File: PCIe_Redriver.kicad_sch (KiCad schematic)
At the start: 56 parts, among them U10 SN75LVPE4410RNQR, U9 SN75LVPE4410RNQR

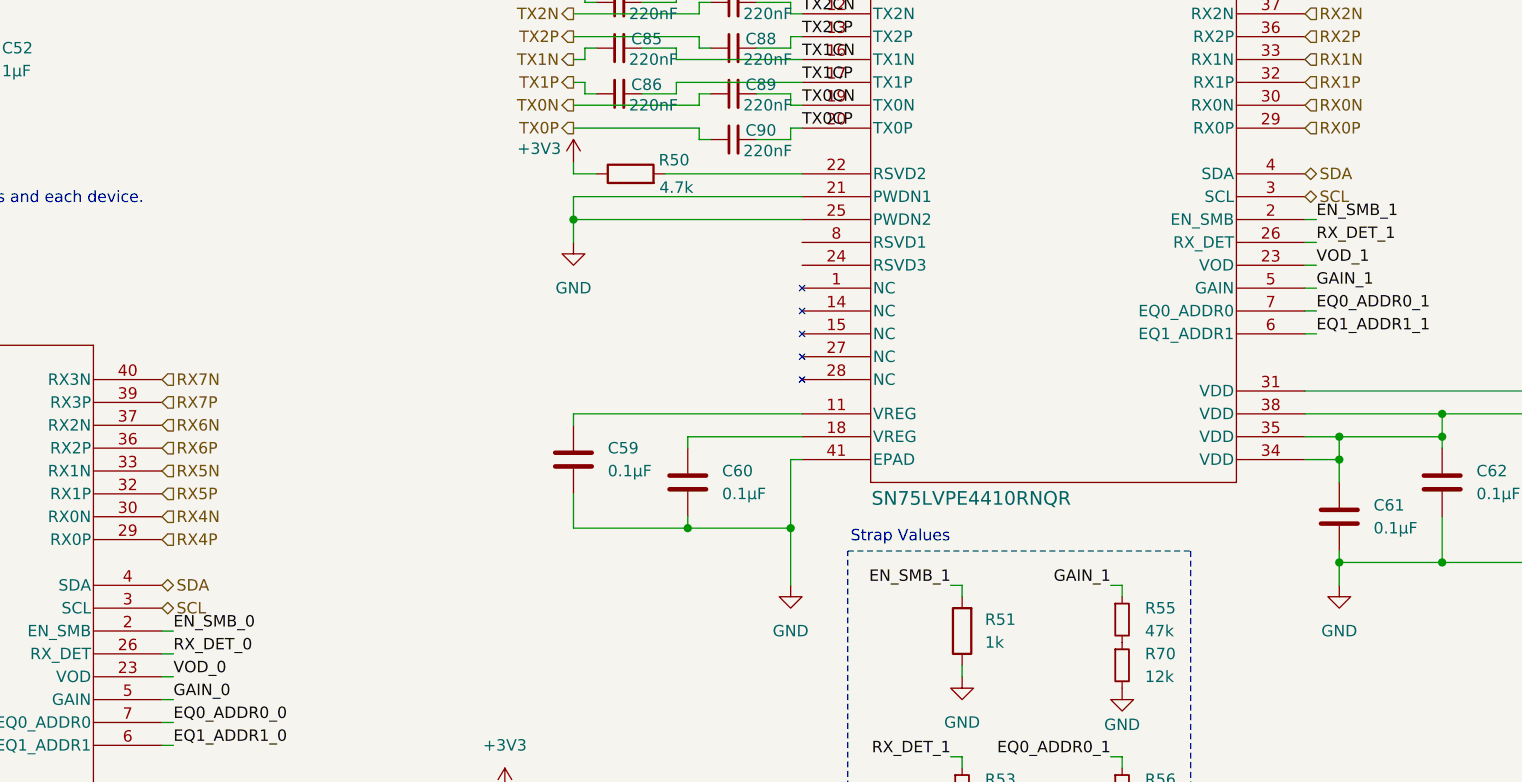
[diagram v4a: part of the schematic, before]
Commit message: Fixed all DRC errors
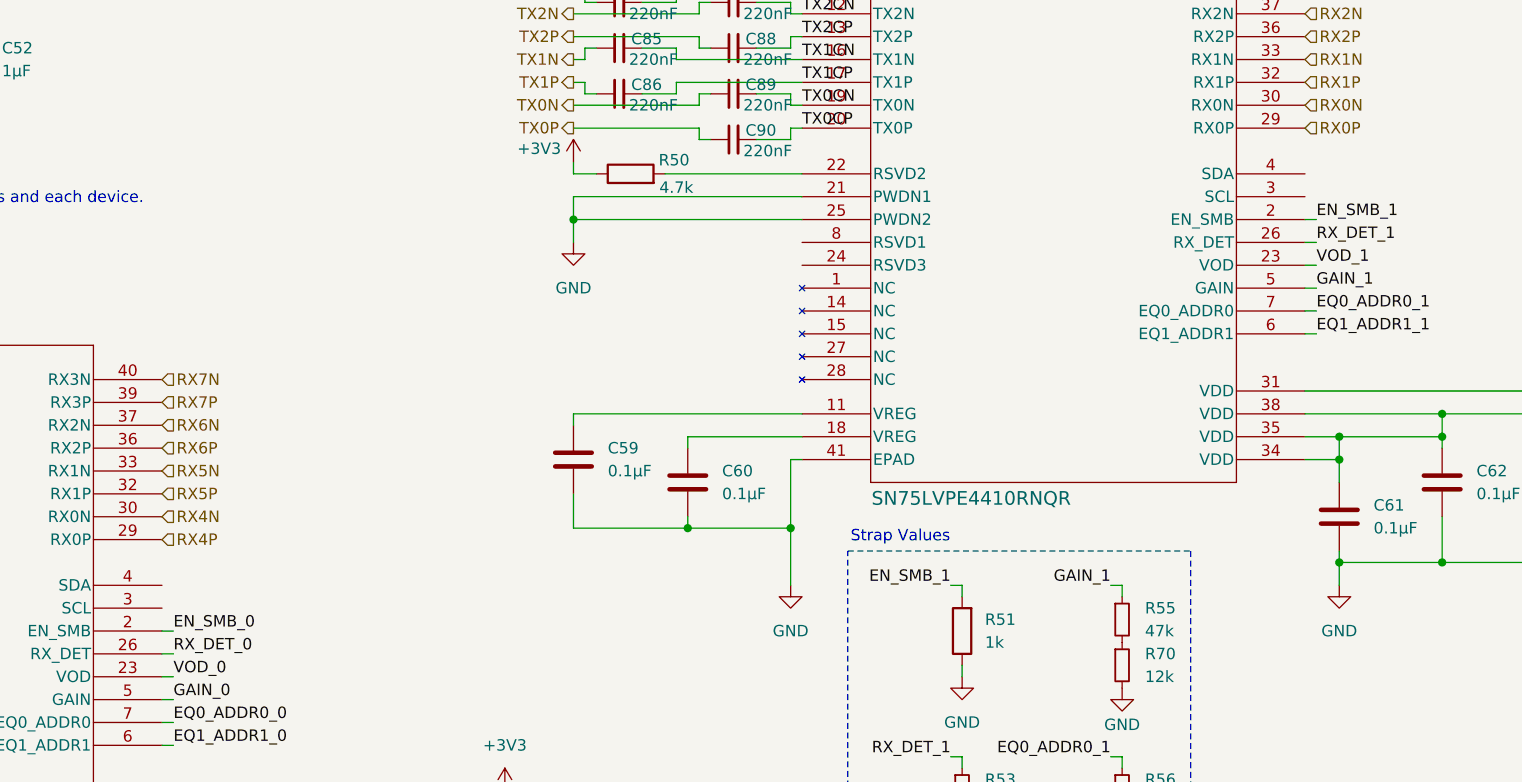
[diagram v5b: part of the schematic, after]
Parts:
- U10, U9: footprint SN75LVPE4410RNQR -> SN75LVPE4410RNQR:SN75LVPE4410RNQR
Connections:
- net SCL: no longer names the net of U9.3 (SCL)
- net SCL: no longer U10.3 (SCL)
- net SDA: no longer names the net of U9.4 (SDA)
- net SDA: no longer U10.4 (SDA)
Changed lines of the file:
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@@
 		)
 	)
-	(hierarchical_label "SDA"
-		(shape bidirectional)
-		(at 107.95 92.71 0)
-		(fields_autoplaced yes)
-		(effects
-			(font
-				(size 1.27 1.27)
-			)
-			(justify left)
-		)
-	)
 	(hierarchical_label "TX3N"
 		(shape output)
@@
 		)
 	)
-	(hierarchical_label "SCL"
-		(shape bidirectional)
-		(at 234.95 49.53 0)
-		(fields_autoplaced yes)
-		(effects
-			(font
-				(size 1.27 1.27)
-			)
-			(justify left)
-		)
-	)
 	(hierarchical_label "TX5N"
 		(shape output)
@@
 		)
 	)
-	(hierarchical_label "SCL"
-		(shape bidirectional)
-		(at 107.95 95.25 0)
-		(fields_autoplaced yes)
-		(effects
-			(font
-				(size 1.27 1.27)
-			)
-			(justify left)
-		)
-	)
 	(hierarchical_label "TX6N"
 		(shape output)
@@
 		)
 	)
-	(hierarchical_label "SDA"
-		(shape bidirectional)
-		(at 234.95 46.99 0)
-		(fields_autoplaced yes)
-		(effects
-			(font
-				(size 1.27 1.27)
-			)
-			(justify left)
-		)
-	)
 	(hierarchical_label "TX2P"
 		(shape output)
@@
 			)
 		)
-		(property "Footprint" "SN75LVPE4410RNQR"
+		(property "Footprint" "SN75LVPE4410RNQR:SN75LVPE4410RNQR"
 			(at 52.07 71.12 0)
 			(effects
@@
 			)
 		)
-		(property "Footprint" "SN75LVPE4410RNQR"
+		(property "Footprint" "SN75LVPE4410RNQR:SN75LVPE4410RNQR"
 			(at 179.07 25.4 0)
 			(effects
